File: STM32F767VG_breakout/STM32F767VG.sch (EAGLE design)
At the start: 31 parts, among them IC1 STM32F767VGT6, IC3 LD117AS33TR, X4 8MHz, X5 32.768kHz, X6 MSTBA2

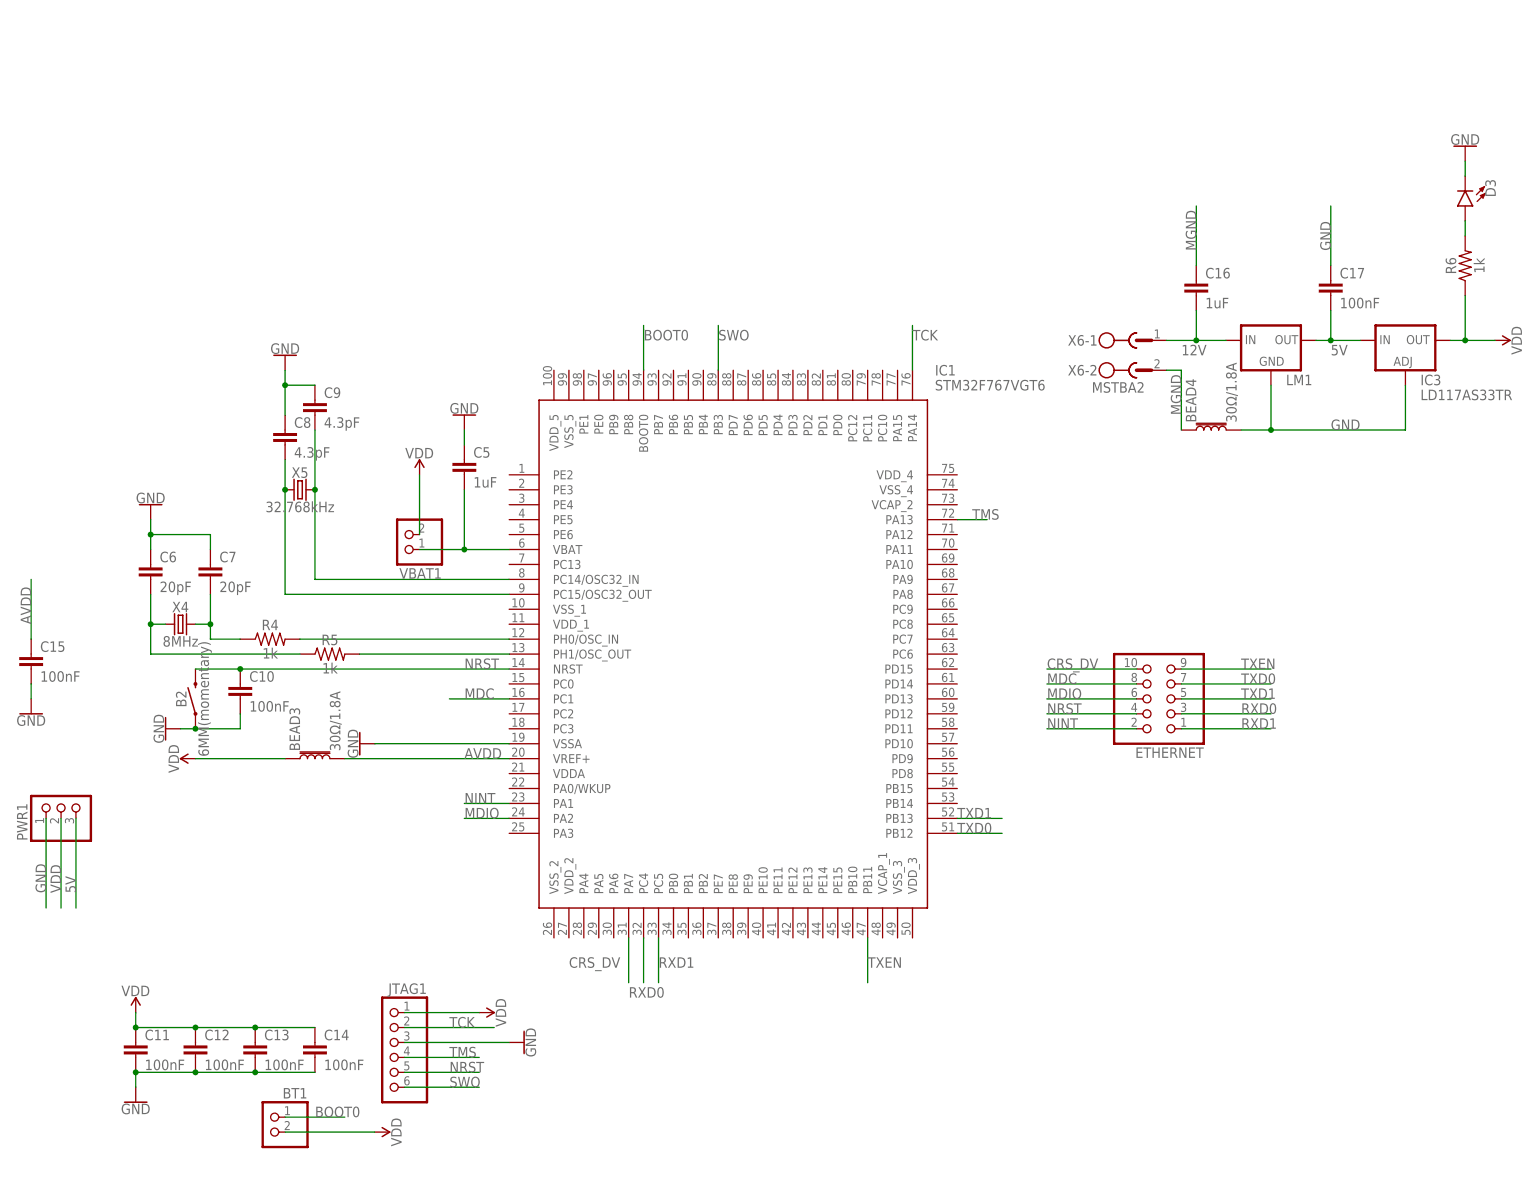
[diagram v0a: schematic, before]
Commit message: First draft of breakout board complete
Pin excel file also updated. For the schematic, added functionality from previous board, connections for ethernet and JTAG, and also exposed all of the other IO pins
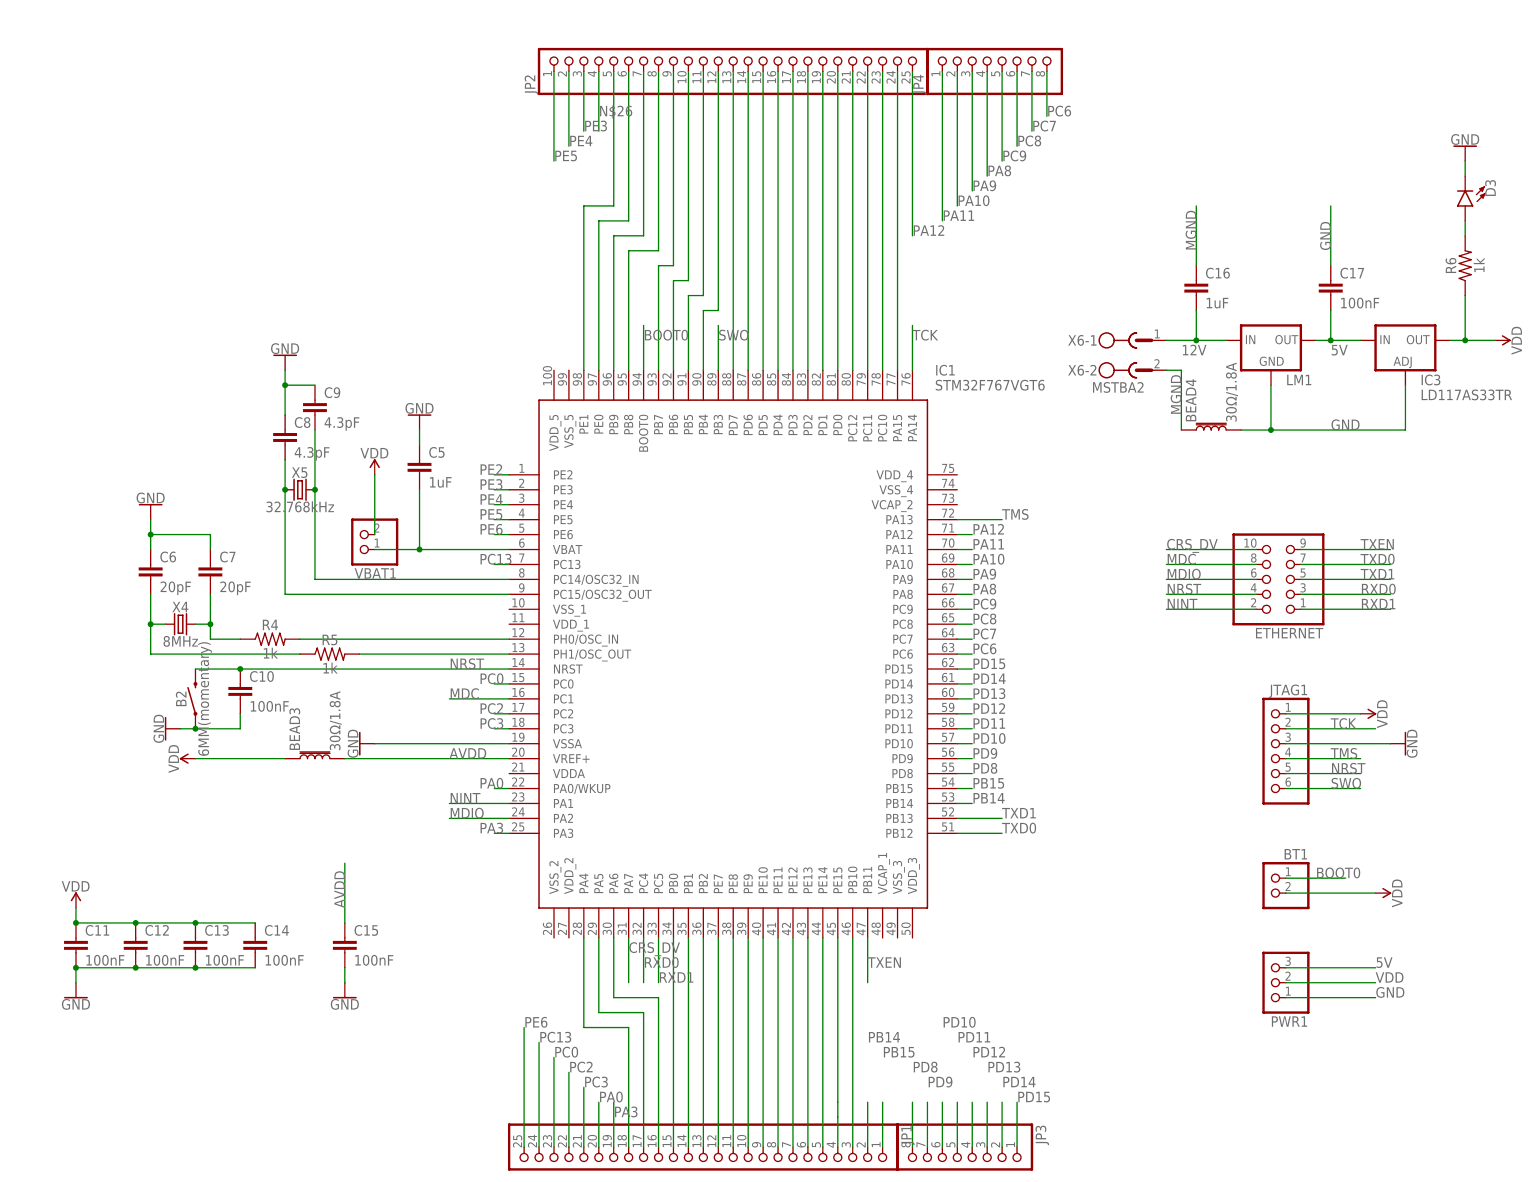
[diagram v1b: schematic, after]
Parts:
- added JP1, JP2: (no value), pinhead:PINHD-1X25
- added JP3, JP4: (no value), pinhead:PINHD-1X8
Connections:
- new net N$1: IC1.PB10, JP1.3
- new net N$10: IC1.PE7, JP1.12
- new net N$11: IC1.PB2, JP1.13
- new net N$12: IC1.PB1, JP1.14
- new net N$18: IC1.PB0, JP1.15
- new net N$2: IC1.PE15, JP1.4
- new net N$20: IC1.PA6, JP1.16
- new net N$24: IC1.PA5, JP1.17
- new net N$25: IC1.PA4, JP1.18
- new net N$26: JP2.4
- new net N$3: IC1.PE14, JP1.5
- new net N$33: IC1.PB6, JP2.10
- new net N$34: IC1.PB7, JP2.9
- new net N$35: IC1.PB8, JP2.8
- new net N$36: IC1.PB9, JP2.7
- new net N$37: IC1.PE0, JP2.6
- new net N$39: IC1.PD7, JP2.13
- new net N$4: IC1.PE13, JP1.6
- new net N$43: IC1.PD3, JP2.17
- new net N$45: IC1.PD1, JP2.19
- new net N$48: IC1.PC11, JP2.22
- new net N$49: IC1.PC10, JP2.23
- new net N$5: IC1.PE12, JP1.7
- new net N$50: IC1.PA15, JP2.24
- new net N$58: IC1.PD6, JP2.14
- new net N$59: IC1.PD5, JP2.15
- new net N$6: IC1.PE11, JP1.8
- new net N$60: IC1.PD4, JP2.16
- new net N$64: IC1.PC12, JP2.21
- new net N$65: IC1.PD0, JP2.20
- new net N$67: IC1.PD2, JP2.18
- new net N$7: IC1.PE10, JP1.9
- new net N$71: IC1.PB5, JP2.11
- new net N$72: IC1.PB4, JP2.12
- new net N$8: IC1.PE9, JP1.10
- new net N$9: IC1.PE8, JP1.11
- new net PA0: IC1.PA0/WKUP, JP1.20
- new net PA10: IC1.PA10, JP4.2
- new net PA11: IC1.PA11, JP4.1
- new net PA12: IC1.PA12, JP2.25
- new net PA3: IC1.PA3, JP1.19
- new net PA8: IC1.PA8, JP4.4
- new net PA9: IC1.PA9, JP4.3
- new net PB14: IC1.PB14, JP1.2
- new net PB15: IC1.PB15, JP1.1
- new net PC0: IC1.PC0, JP1.23
- new net PC13: IC1.PC13, JP1.24
- new net PC2: IC1.PC2, JP1.22
- new net PC3: IC1.PC3, JP1.21
- new net PC6: IC1.PC6, JP4.8
- new net PC7: IC1.PC7, JP4.7
- new net PC8: IC1.PC8, JP4.6
- new net PC9: IC1.PC9, JP4.5
- new net PD10: IC1.PD10, JP3.6
- new net PD11: IC1.PD11, JP3.5
- new net PD12: IC1.PD12, JP3.4
- new net PD13: IC1.PD13, JP3.3
- new net PD14: IC1.PD14, JP3.2
- new net PD15: IC1.PD15, JP3.1
- new net PD8: IC1.PD8, JP3.8
- new net PD9: IC1.PD9, JP3.7
- new net PE2: IC1.PE1, IC1.PE2, JP2.5
- new net PE3: IC1.PE3, JP2.3
- new net PE4: IC1.PE4, JP2.2
- new net PE5: IC1.PE5, JP2.1
- new net PE6: IC1.PE6, JP1.25
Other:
- moved on the sheet: BT1, C11, C12, C13, C14, C15, C5, ETHERNET, JTAG1, PWR1, VBAT1

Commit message: Revised ethernet connections
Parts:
- added R1: 10k, SparkFun-Resistors:10KOHM-HORIZ-1/4W-1%
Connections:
- removed net N$26: JP2.4
- net CRS_DV: now also ETHERNET.3; no longer ETHERNET.10
- net MDC: now also ETHERNET.2; no longer ETHERNET.8
- net MDIO: now also ETHERNET.9; no longer ETHERNET.6
- net NINT: now also ETHERNET.1; no longer ETHERNET.2
- net NRST: now also R1.2
- net PE2: now also JP2.4
- net RXD0: now also ETHERNET.5; no longer ETHERNET.3
- net RXD1: now also ETHERNET.7; no longer ETHERNET.1
- net TXD0: now also ETHERNET.8; no longer ETHERNET.7
- net TXD1: now also ETHERNET.10; no longer ETHERNET.5
- net TXEN: now also ETHERNET.6; no longer ETHERNET.9
- net VDD: now also R1.1

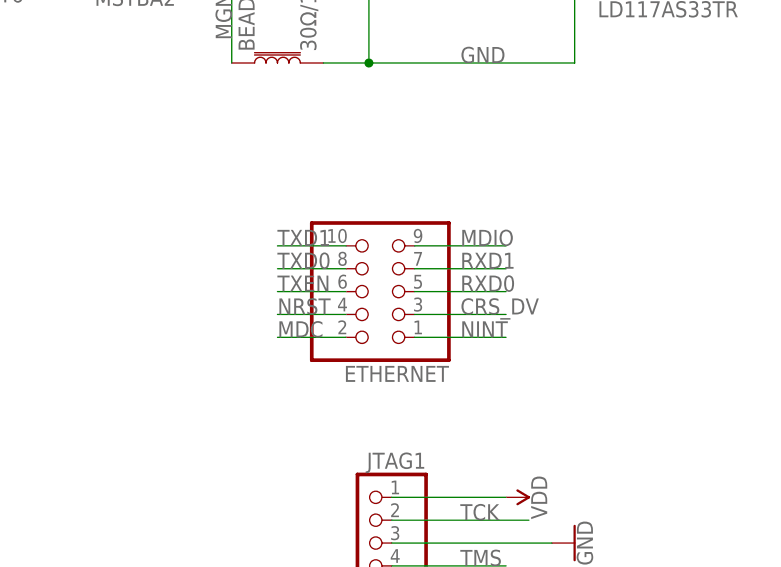
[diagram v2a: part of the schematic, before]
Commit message: Updated Ethernet Connection part
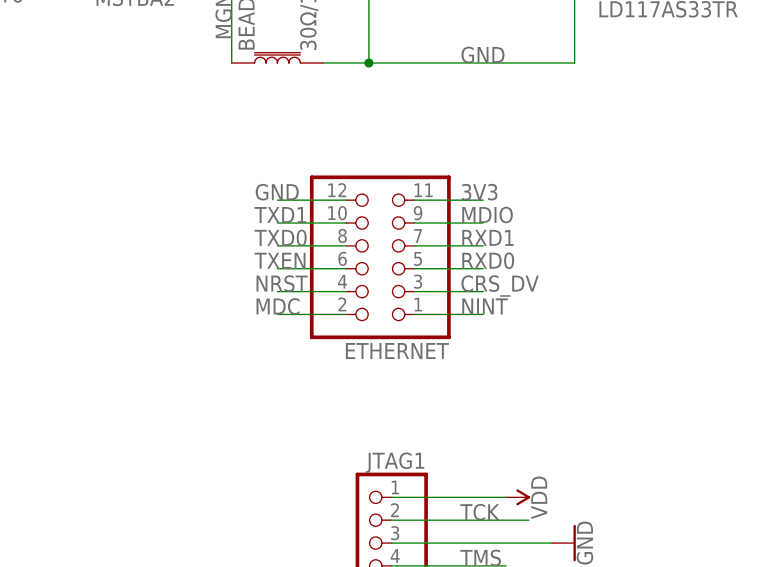
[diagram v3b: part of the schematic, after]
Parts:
- ETHERNET: device pinhead:PINHD-2X5 -> pinhead:PINHD-2X6
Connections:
- new net 3V3: ETHERNET.11
- net GND: now also ETHERNET.12
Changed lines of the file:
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@@
 <part name="GND30" library="SparkFun-PowerSymbols" deviceset="GND" device=""/>
 <part name="GND31" library="SparkFun-PowerSymbols" deviceset="GND" device=""/>
-<part name="ETHERNET" library="pinhead" library_urn="urn:adsk.eagle:library:325" deviceset="PINHD-2X5" device="" package3d_urn="urn:adsk.eagle:package:22470/2"/>
 <part name="PWR1" library="pinhead" library_urn="urn:adsk.eagle:library:325" deviceset="PINHD-1X3" device="" package3d_urn="urn:adsk.eagle:package:22458/2"/>
 <part name="C15" library="ee2parts" deviceset="C" device="2.5P" value="100nF"/>
@@
 <part name="SUPPLY1" library="SparkFun-PowerSymbols" deviceset="VDD" device=""/>
 <part name="R1" library="SparkFun-Resistors" deviceset="10KOHM" device="-HORIZ-1/4W-1%" value="10k"/>
+<part name="ETHERNET" library="pinhead" library_urn="urn:adsk.eagle:library:325" deviceset="PINHD-2X6" device="" package3d_urn="urn:adsk.eagle:package:22474/2"/>
 </parts>
 <sheets>
@@
 <instance part="GND30" gate="1" x="-73.66" y="-88.9"/>
 <instance part="GND31" gate="1" x="152.4" y="-45.72" rot="R90"/>
-<instance part="ETHERNET" gate="A" x="132.08" y="-17.78" rot="R180"/>
 <instance part="PWR1" gate="A" x="129.54" y="-86.36" rot="R180"/>
 <instance part="C15" gate="G$1" x="-27.94" y="-81.28"/>
@@
 <instance part="SUPPLY1" gate="VDD" x="-76.2" y="-33.02" rot="R90"/>
 <instance part="R1" gate="G$1" x="-66.04" y="-33.02"/>
+<instance part="ETHERNET" gate="A" x="132.08" y="-15.24" rot="R180"/>
 </instances>
 <busses>
@@
 <pinref part="D3" gate="G$1" pin="C"/>
 </segment>
+<segment>
+<pinref part="ETHERNET" gate="A" pin="12"/>
+<wire x1="127" y1="-7.62" x2="119.38" y2="-7.62" width="0.1524" layer="91"/>
+<label x="116.84" y="-7.62" size="1.778" layer="95"/>
+</segment>
 </net>
 <net name="VDD" class="0">
@@
 <segment>
 <pinref part="ETHERNET" gate="A" pin="4"/>
-<wire x1="127" y1="-20.32" x2="119.38" y2="-20.32" width="0.1524" layer="91"/>
-<label x="119.38" y="-20.32" size="1.778" layer="95"/>
+<wire x1="127" y1="-17.78" x2="119.38" y2="-17.78" width="0.1524" layer="91"/>
+<label x="116.84" y="-17.78" size="1.778" layer="95"/>
 </segment>
 </net>
@@
 <segment>
 <pinref part="ETHERNET" gate="A" pin="8"/>
-<wire x1="127" y1="-15.24" x2="119.38" y2="-15.24" width="0.1524" layer="91"/>
-<label x="119.38" y="-15.24" size="1.778" layer="95"/>
+<wire x1="127" y1="-12.7" x2="119.38" y2="-12.7" width="0.1524" layer="91"/>
+<label x="116.84" y="-12.7" size="1.778" layer="95"/>
 </segment>
 </net>
@@
 <segment>
 <pinref part="ETHERNET" gate="A" pin="10"/>
-<wire x1="127" y1="-12.7" x2="119.38" y2="-12.7" width="0.1524" layer="91"/>
-<label x="119.38" y="-12.7" size="1.778" layer="95"/>
+<wire x1="127" y1="-10.16" x2="119.38" y2="-10.16" width="0.1524" layer="91"/>
+<label x="116.84" y="-10.16" size="1.778" layer="95"/>
 </segment>
 </net>
@@
 <segment>
 <pinref part="ETHERNET" gate="A" pin="6"/>
-<wire x1="127" y1="-17.78" x2="119.38" y2="-17.78" width="0.1524" layer="91"/>
-<label x="119.38" y="-17.78" size="1.778" layer="95"/>
+<wire x1="127" y1="-15.24" x2="119.38" y2="-15.24" width="0.1524" layer="91"/>
+<label x="116.84" y="-15.24" size="1.778" layer="95"/>
 </segment>
 </net>
@@
 <segment>
 <pinref part="ETHERNET" gate="A" pin="5"/>
-<wire x1="134.62" y1="-17.78" x2="144.78" y2="-17.78" width="0.1524" layer="91"/>
-<label x="139.7" y="-17.78" size="1.778" layer="95"/>
+<wire x1="134.62" y1="-15.24" x2="142.24" y2="-15.24" width="0.1524" layer="91"/>
+<label x="139.7" y="-15.24" size="1.778" layer="95"/>
 </segment>
 </net>
@@
 <segment>
 <pinref part="ETHERNET" gate="A" pin="7"/>
-<wire x1="134.62" y1="-15.24" x2="144.78" y2="-15.24" width="0.1524" layer="91"/>
-<label x="139.7" y="-15.24" size="1.778" layer="95"/>
+<wire x1="134.62" y1="-12.7" x2="142.24" y2="-12.7" width="0.1524" layer="91"/>
+<label x="139.7" y="-12.7" size="1.778" layer="95"/>
 </segment>
 </net>
@@
 <segment>
 <pinref part="ETHERNET" gate="A" pin="9"/>
-<wire x1="134.62" y1="-12.7" x2="144.78" y2="-12.7" width="0.1524" layer="91"/>
-<label x="139.7" y="-12.7" size="1.778" layer="95"/>
+<wire x1="134.62" y1="-10.16" x2="142.24" y2="-10.16" width="0.1524" layer="91"/>
+<label x="139.7" y="-10.16" size="1.778" layer="95"/>
 </segment>
 </net>
@@
 <segment>
 <pinref part="ETHERNET" gate="A" pin="2"/>
-<wire x1="127" y1="-22.86" x2="119.38" y2="-22.86" width="0.1524" layer="91"/>
-<label x="119.38" y="-22.86" size="1.778" layer="95"/>
+<wire x1="127" y1="-20.32" x2="119.38" y2="-20.32" width="0.1524" layer="91"/>
+<label x="116.84" y="-20.32" size="1.778" layer="95"/>
 </segment>
 </net>
@@
 <segment>
 <pinref part="ETHERNET" gate="A" pin="1"/>
-<wire x1="134.62" y1="-22.86" x2="144.78" y2="-22.86" width="0.1524" layer="91"/>
-<label x="139.7" y="-22.86" size="1.778" layer="95"/>
+<wire x1="134.62" y1="-20.32" x2="142.24" y2="-20.32" width="0.1524" layer="91"/>
+<label x="139.7" y="-20.32" size="1.778" layer="95"/>
 </segment>
 </net>
@@
 <segment>
 <pinref part="ETHERNET" gate="A" pin="3"/>
-<wire x1="134.62" y1="-20.32" x2="144.78" y2="-20.32" width="0.1524" layer="91"/>
-<label x="139.7" y="-20.32" size="1.778" layer="95"/>
+<wire x1="134.62" y1="-17.78" x2="142.24" y2="-17.78" width="0.1524" layer="91"/>
+<label x="139.7" y="-17.78" size="1.778" layer="95"/>
 </segment>
 </net>
@@
 </segment>
 </net>
+<net name="3V3" class="0">
+<segment>
+<pinref part="ETHERNET" gate="A" pin="11"/>
+<wire x1="134.62" y1="-7.62" x2="142.24" y2="-7.62" width="0.1524" layer="91"/>
+<label x="139.7" y="-7.62" size="1.778" layer="95"/>
+</segment>
+</net>
